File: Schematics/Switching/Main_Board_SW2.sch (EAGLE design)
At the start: 83 parts, among them IC3 SWITCHER, IC4 SWITCHER, Q1 32.768kHz, X1 MINI-USB-SHIELD-UX60-MB-5ST, X2 RJ45

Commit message: PCB Push
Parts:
- added R28, R29: 5.6k, rcl:R-US_R0805
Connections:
- new net N$22: R28.1, R29.2, U$1.5
- net GND: now also R29.1
- net V+: now also R28.2
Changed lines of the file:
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@@
 <?xml version="1.0" encoding="utf-8"?>
 <!DOCTYPE eagle SYSTEM "eagle.dtd">
-<eagle version="6.5.0">
+<eagle version="6.3">
 <drawing>
 <settings>
@@
 <grid distance="0.1" unitdist="inch" unit="inch" style="lines" multiple="1" display="no" altdistance="0.01" altunitdist="inch" altunit="inch"/>
 <layers>
-<layer number="1" name="Top" color="4" fill="1" visible="no" active="no"/>
-<layer number="16" name="Bottom" color="1" fill="1" visible="no" active="no"/>
-<layer number="17" name="Pads" color="2" fill="1" visible="no" active="no"/>
-<layer number="18" name="Vias" color="2" fill="1" visible="no" active="no"/>
-<layer number="19" name="Unrouted" color="6" fill="1" visible="no" active="no"/>
-<layer number="20" name="Dimension" color="15" fill="1" visible="no" active="no"/>
-<layer number="21" name="tPlace" color="7" fill="1" visible="no" active="no"/>
-<layer number="22" name="bPlace" color="7" fill="1" visible="no" active="no"/>
-<layer number="23" name="tOrigins" color="15" fill="1" visible="no" active="no"/>
-<layer number="24" name="bOrigins" color="15" fill="1" visible="no" active="no"/>
-<layer number="25" name="tNames" color="7" fill="1" visible="no" active="no"/>
-<layer number="26" name="bNames" color="7" fill="1" visible="no" active="no"/>
-<layer number="27" name="tValues" color="7" fill="1" visible="no" active="no"/>
-<layer number="28" name="bValues" color="7" fill="1" visible="no" active="no"/>
+<layer number="1" name="Top" color="4" fill="1" visible="yes" active="no"/>
+<layer number="16" name="Bottom" color="1" fill="1" visible="yes" active="no"/>
+<layer number="17" name="Pads" color="2" fill="1" visible="yes" active="no"/>
+<layer number="18" name="Vias" color="2" fill="1" visible="yes" active="no"/>
+<layer number="19" name="Unrouted" color="6" fill="1" visible="yes" active="no"/>
+<layer number="20" name="Dimension" color="15" fill="1" visible="yes" active="no"/>
+<layer number="21" name="tPlace" color="7" fill="1" visible="yes" active="no"/>
+<layer number="22" name="bPlace" color="7" fill="1" visible="yes" active="no"/>
+<layer number="23" name="tOrigins" color="15" fill="1" visible="yes" active="no"/>
+<layer number="24" name="bOrigins" color="15" fill="1" visible="yes" active="no"/>
+<layer number="25" name="tNames" color="7" fill="1" visible="yes" active="no"/>
+<layer number="26" name="bNames" color="7" fill="1" visible="yes" active="no"/>
+<layer number="27" name="tValues" color="7" fill="1" visible="yes" active="no"/>
+<layer number="28" name="bValues" color="7" fill="1" visible="yes" active="no"/>
 <layer number="29" name="tStop" color="7" fill="3" visible="no" active="no"/>
 <layer number="30" name="bStop" color="7" fill="6" visible="no" active="no"/>
@@
 <layer number="35" name="tGlue" color="7" fill="4" visible="no" active="no"/>
 <layer number="36" name="bGlue" color="7" fill="5" visible="no" active="no"/>
-<layer number="37" name="tTest" color="7" fill="1" visible="no" active="no"/>
-<layer number="38" name="bTest" color="7" fill="1" visible="no" active="no"/>
+<layer number="37" name="tTest" color="7" fill="1" visible="yes" active="no"/>
+<layer number="38" name="bTest" color="7" fill="1" visible="yes" active="no"/>
 <layer number="39" name="tKeepout" color="4" fill="11" visible="no" active="no"/>
 <layer number="40" name="bKeepout" color="1" fill="11" visible="no" active="no"/>
@@
 <layer number="44" name="Drills" color="7" fill="1" visible="no" active="no"/>
 <layer number="45" name="Holes" color="7" fill="1" visible="no" active="no"/>
-<layer number="46" name="Milling" color="3" fill="1" visible="no" active="no"/>
-<layer number="47" name="Measures" color="7" fill="1" visible="no" active="no"/>
-<layer number="48" name="Document" color="7" fill="1" visible="no" active="no"/>
-<layer number="49" name="Reference" color="7" fill="1" visible="no" active="no"/>
-<layer number="50" name="dxf" color="7" fill="1" visible="no" active="no"/>
-<layer number="51" name="tDocu" color="7" fill="1" visible="no" active="no"/>
-<layer number="52" name="bDocu" color="7" fill="1" visible="no" active="no"/>
-<layer number="53" name="tGND_GNDA" color="7" fill="1" visible="no" active="no"/>
-<layer number="54" name="bGND_GNDA" color="7" fill="1" visible="no" active="no"/>
-<layer number="56" name="wert" color="7" fill="1" visible="no" active="no"/>
+<layer number="46" name="Milling" color="3" fill="1" visible="yes" active="no"/>
+<layer number="47" name="Measures" color="7" fill="1" visible="yes" active="no"/>
+<layer number="48" name="Document" color="7" fill="1" visible="yes" active="no"/>
+<layer number="49" name="Reference" color="7" fill="1" visible="yes" active="no"/>
+<layer number="50" name="dxf" color="7" fill="1" visible="yes" active="no"/>
+<layer number="51" name="tDocu" color="7" fill="1" visible="yes" active="no"/>
+<layer number="52" name="bDocu" color="7" fill="1" visible="yes" active="no"/>
+<layer number="53" name="tGND_GNDA" color="7" fill="1" visible="yes" active="no"/>
+<layer number="54" name="bGND_GNDA" color="7" fill="1" visible="yes" active="no"/>
+<layer number="56" name="wert" color="7" fill="1" visible="yes" active="no"/>
 <layer number="91" name="Nets" color="2" fill="1" visible="yes" active="yes"/>
 <layer number="92" name="Busses" color="1" fill="1" visible="yes" active="yes"/>
@@
 <part name="H3" library="holes" deviceset="MOUNT-HOLE" device="2.8"/>
 <part name="H4" library="holes" deviceset="MOUNT-HOLE" device="2.8"/>
+<part name="R28" library="rcl" deviceset="R-US_" device="R0805" value="5.6k"/>
+<part name="R29" library="rcl" deviceset="R-US_" device="R0805" value="5.6k"/>
+<part name="SUPPLY1" library="supply2" deviceset="V+" device=""/>
+<part name="GND14" library="supply1" deviceset="GND" device=""/>
 </parts>
 <sheets>
@@
 <instance part="H3" gate="G$1" x="185.42" y="0"/>
 <instance part="H4" gate="G$1" x="185.42" y="-5.08"/>
+<instance part="R28" gate="G$1" x="10.16" y="68.58" smashed="yes" rot="R90">
+<attribute name="NAME" x="8.6614" y="64.77" size="1.778" layer="95" rot="R90"/>
+<attribute name="VALUE" x="13.462" y="64.77" size="1.778" layer="96" rot="R90"/>
+</instance>
+<instance part="R29" gate="G$1" x="10.16" y="55.88" smashed="yes" rot="R90">
+<attribute name="NAME" x="8.6614" y="52.07" size="1.778" layer="95" rot="R90"/>
+<attribute name="VALUE" x="13.462" y="52.07" size="1.778" layer="96" rot="R90"/>
+</instance>
+<instance part="SUPPLY1" gate="1" x="10.16" y="78.74"/>
+<instance part="GND14" gate="1" x="10.16" y="45.72"/>
 </instances>
 <busses>
@@
 <junction x="109.22" y="68.58"/>
 </segment>
+<segment>
+<pinref part="GND14" gate="1" pin="GND"/>
+<pinref part="R29" gate="G$1" pin="1"/>
+<wire x1="10.16" y1="50.8" x2="10.16" y2="48.26" width="0.1524" layer="91"/>
+</segment>
 </net>
 <net name="N$11" class="0">
@@
 <pinref part="SUPPLY8" gate="1" pin="V+"/>
 </segment>
+<segment>
+<pinref part="SUPPLY1" gate="1" pin="V+"/>
+<pinref part="R28" gate="G$1" pin="2"/>
+<wire x1="10.16" y1="76.2" x2="10.16" y2="73.66" width="0.1524" layer="91"/>
+</segment>
 </net>
 <net name="N$13" class="0">
@@
 </segment>
 </net>
+<net name="N$22" class="0">
+<segment>
+<wire x1="15.24" y1="60.96" x2="15.24" y2="81.28" width="0.1524" layer="91"/>
+<pinref part="R28" gate="G$1" pin="1"/>
+<pinref part="R29" gate="G$1" pin="2"/>
+<wire x1="10.16" y1="60.96" x2="10.16" y2="63.5" width="0.1524" layer="91"/>
+<wire x1="10.16" y1="60.96" x2="15.24" y2="60.96" width="0.1524" layer="91"/>
+<junction x="10.16" y="60.96"/>
+<wire x1="15.24" y1="81.28" x2="33.02" y2="81.28" width="0.1524" layer="91"/>
+<wire x1="33.02" y1="81.28" x2="33.02" y2="63.5" width="0.1524" layer="91"/>
+<pinref part="U$1" gate="G$1" pin="5"/>
+<wire x1="33.02" y1="63.5" x2="53.34" y2="63.5" width="0.1524" layer="91"/>
+</segment>
+</net>

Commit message: PCB Verified. Add Battery Sense
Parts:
- R16, R19: device resistor:R-US_R1206 -> resistor:R-US_R0805
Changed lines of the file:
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@@
 <part name="IC3" library="linear-technology-2" deviceset="SWITCHER" device=""/>
 <part name="SUPPLY4" library="supply2" deviceset="V+" device=""/>
-<part name="R16" library="resistor" deviceset="R-US_" device="R1206" value="499K"/>
+<part name="R16" library="resistor" deviceset="R-US_" device="R0805" value="499K"/>
 <part name="R17" library="rcl" deviceset="R-US_" device="R0805" value="10k"/>
 <part name="L1" library="Inductor" deviceset="SHEILDED_COIL" device="" value="4.7uH"/>
@@
 <part name="IC4" library="linear-technology-2" deviceset="SWITCHER" device=""/>
 <part name="SUPPLY6" library="supply2" deviceset="V+" device=""/>
-<part name="R19" library="resistor" deviceset="R-US_" device="R1206" value="499k"/>
+<part name="R19" library="resistor" deviceset="R-US_" device="R0805" value="499k"/>
 <part name="R20" library="rcl" deviceset="R-US_" device="R0805" value="10k"/>
 <part name="L2" library="Inductor" deviceset="SHEILDED_COIL" device="" value="4.7uH"/>

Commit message: Last layout sync of night
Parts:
- L1: value 4.7uH -> 3.3uH
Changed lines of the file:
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@@
 <?xml version="1.0" encoding="utf-8"?>
 <!DOCTYPE eagle SYSTEM "eagle.dtd">
-<eagle version="6.3">
+<eagle version="6.4">
 <drawing>
 <settings>
@@
 <grid distance="0.1" unitdist="inch" unit="inch" style="lines" multiple="1" display="no" altdistance="0.01" altunitdist="inch" altunit="inch"/>
 <layers>
-<layer number="1" name="Top" color="4" fill="1" visible="yes" active="no"/>
-<layer number="16" name="Bottom" color="1" fill="1" visible="yes" active="no"/>
-<layer number="17" name="Pads" color="2" fill="1" visible="yes" active="no"/>
-<layer number="18" name="Vias" color="2" fill="1" visible="yes" active="no"/>
-<layer number="19" name="Unrouted" color="6" fill="1" visible="yes" active="no"/>
-<layer number="20" name="Dimension" color="15" fill="1" visible="yes" active="no"/>
-<layer number="21" name="tPlace" color="7" fill="1" visible="yes" active="no"/>
-<layer number="22" name="bPlace" color="7" fill="1" visible="yes" active="no"/>
-<layer number="23" name="tOrigins" color="15" fill="1" visible="yes" active="no"/>
-<layer number="24" name="bOrigins" color="15" fill="1" visible="yes" active="no"/>
-<layer number="25" name="tNames" color="7" fill="1" visible="yes" active="no"/>
-<layer number="26" name="bNames" color="7" fill="1" visible="yes" active="no"/>
-<layer number="27" name="tValues" color="7" fill="1" visible="yes" active="no"/>
-<layer number="28" name="bValues" color="7" fill="1" visible="yes" active="no"/>
+<layer number="1" name="Top" color="4" fill="1" visible="no" active="no"/>
+<layer number="16" name="Bottom" color="1" fill="1" visible="no" active="no"/>
+<layer number="17" name="Pads" color="2" fill="1" visible="no" active="no"/>
+<layer number="18" name="Vias" color="2" fill="1" visible="no" active="no"/>
+<layer number="19" name="Unrouted" color="6" fill="1" visible="no" active="no"/>
+<layer number="20" name="Dimension" color="15" fill="1" visible="no" active="no"/>
+<layer number="21" name="tPlace" color="7" fill="1" visible="no" active="no"/>
+<layer number="22" name="bPlace" color="7" fill="1" visible="no" active="no"/>
+<layer number="23" name="tOrigins" color="15" fill="1" visible="no" active="no"/>
+<layer number="24" name="bOrigins" color="15" fill="1" visible="no" active="no"/>
+<layer number="25" name="tNames" color="7" fill="1" visible="no" active="no"/>
+<layer number="26" name="bNames" color="7" fill="1" visible="no" active="no"/>
+<layer number="27" name="tValues" color="7" fill="1" visible="no" active="no"/>
+<layer number="28" name="bValues" color="7" fill="1" visible="no" active="no"/>
 <layer number="29" name="tStop" color="7" fill="3" visible="no" active="no"/>
 <layer number="30" name="bStop" color="7" fill="6" visible="no" active="no"/>
@@
 <layer number="35" name="tGlue" color="7" fill="4" visible="no" active="no"/>
 <layer number="36" name="bGlue" color="7" fill="5" visible="no" active="no"/>
-<layer number="37" name="tTest" color="7" fill="1" visible="yes" active="no"/>
-<layer number="38" name="bTest" color="7" fill="1" visible="yes" active="no"/>
+<layer number="37" name="tTest" color="7" fill="1" visible="no" active="no"/>
+<layer number="38" name="bTest" color="7" fill="1" visible="no" active="no"/>
 <layer number="39" name="tKeepout" color="4" fill="11" visible="no" active="no"/>
 <layer number="40" name="bKeepout" color="1" fill="11" visible="no" active="no"/>
@@
 <layer number="44" name="Drills" color="7" fill="1" visible="no" active="no"/>
 <layer number="45" name="Holes" color="7" fill="1" visible="no" active="no"/>
-<layer number="46" name="Milling" color="3" fill="1" visible="yes" active="no"/>
-<layer number="47" name="Measures" color="7" fill="1" visible="yes" active="no"/>
-<layer number="48" name="Document" color="7" fill="1" visible="yes" active="no"/>
-<layer number="49" name="Reference" color="7" fill="1" visible="yes" active="no"/>
-<layer number="50" name="dxf" color="7" fill="1" visible="yes" active="no"/>
-<layer number="51" name="tDocu" color="7" fill="1" visible="yes" active="no"/>
-<layer number="52" name="bDocu" color="7" fill="1" visible="yes" active="no"/>
-<layer number="53" name="tGND_GNDA" color="7" fill="1" visible="yes" active="no"/>
-<layer number="54" name="bGND_GNDA" color="7" fill="1" visible="yes" active="no"/>
-<layer number="56" name="wert" color="7" fill="1" visible="yes" active="no"/>
+<layer number="46" name="Milling" color="3" fill="1" visible="no" active="no"/>
+<layer number="47" name="Measures" color="7" fill="1" visible="no" active="no"/>
+<layer number="48" name="Document" color="7" fill="1" visible="no" active="no"/>
+<layer number="49" name="Reference" color="7" fill="1" visible="no" active="no"/>
+<layer number="50" name="dxf" color="7" fill="1" visible="no" active="no"/>
+<layer number="51" name="tDocu" color="7" fill="1" visible="no" active="no"/>
+<layer number="52" name="bDocu" color="7" fill="1" visible="no" active="no"/>
+<layer number="53" name="tGND_GNDA" color="7" fill="1" visible="no" active="no"/>
+<layer number="54" name="bGND_GNDA" color="7" fill="1" visible="no" active="no"/>
+<layer number="56" name="wert" color="7" fill="1" visible="no" active="no"/>
 <layer number="91" name="Nets" color="2" fill="1" visible="yes" active="yes"/>
 <layer number="92" name="Busses" color="1" fill="1" visible="yes" active="yes"/>
@@
 <part name="R16" library="resistor" deviceset="R-US_" device="R0805" value="499K"/>
 <part name="R17" library="rcl" deviceset="R-US_" device="R0805" value="10k"/>
-<part name="L1" library="Inductor" deviceset="SHEILDED_COIL" device="" value="4.7uH"/>
+<part name="L1" library="Inductor" deviceset="SHEILDED_COIL" device="" value="3.3uH"/>
 <part name="D6" library="diode" deviceset="DIODE-" device="SOD323-R"/>
 <part name="D7" library="diode" deviceset="DIODE-" device="SOD323-R"/>

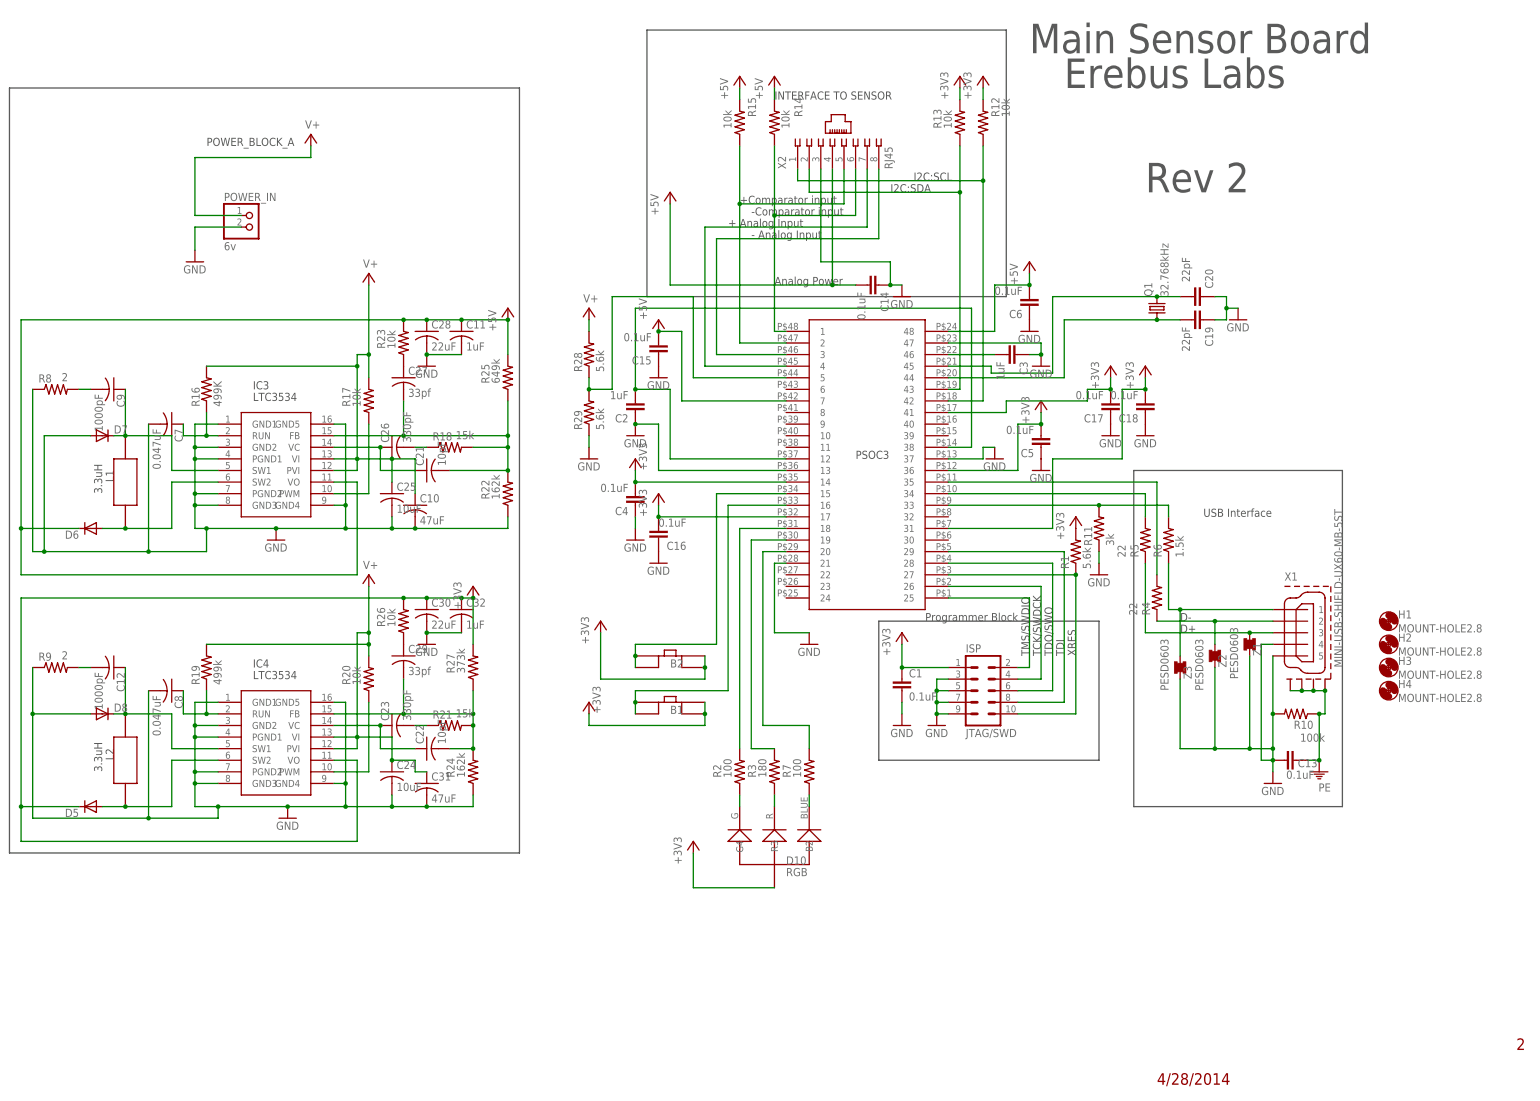
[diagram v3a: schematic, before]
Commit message: Cleaned up stuff
Made Schematics easier to read
Split Supplies in BOM and made names match references
Renamed parts on sensor
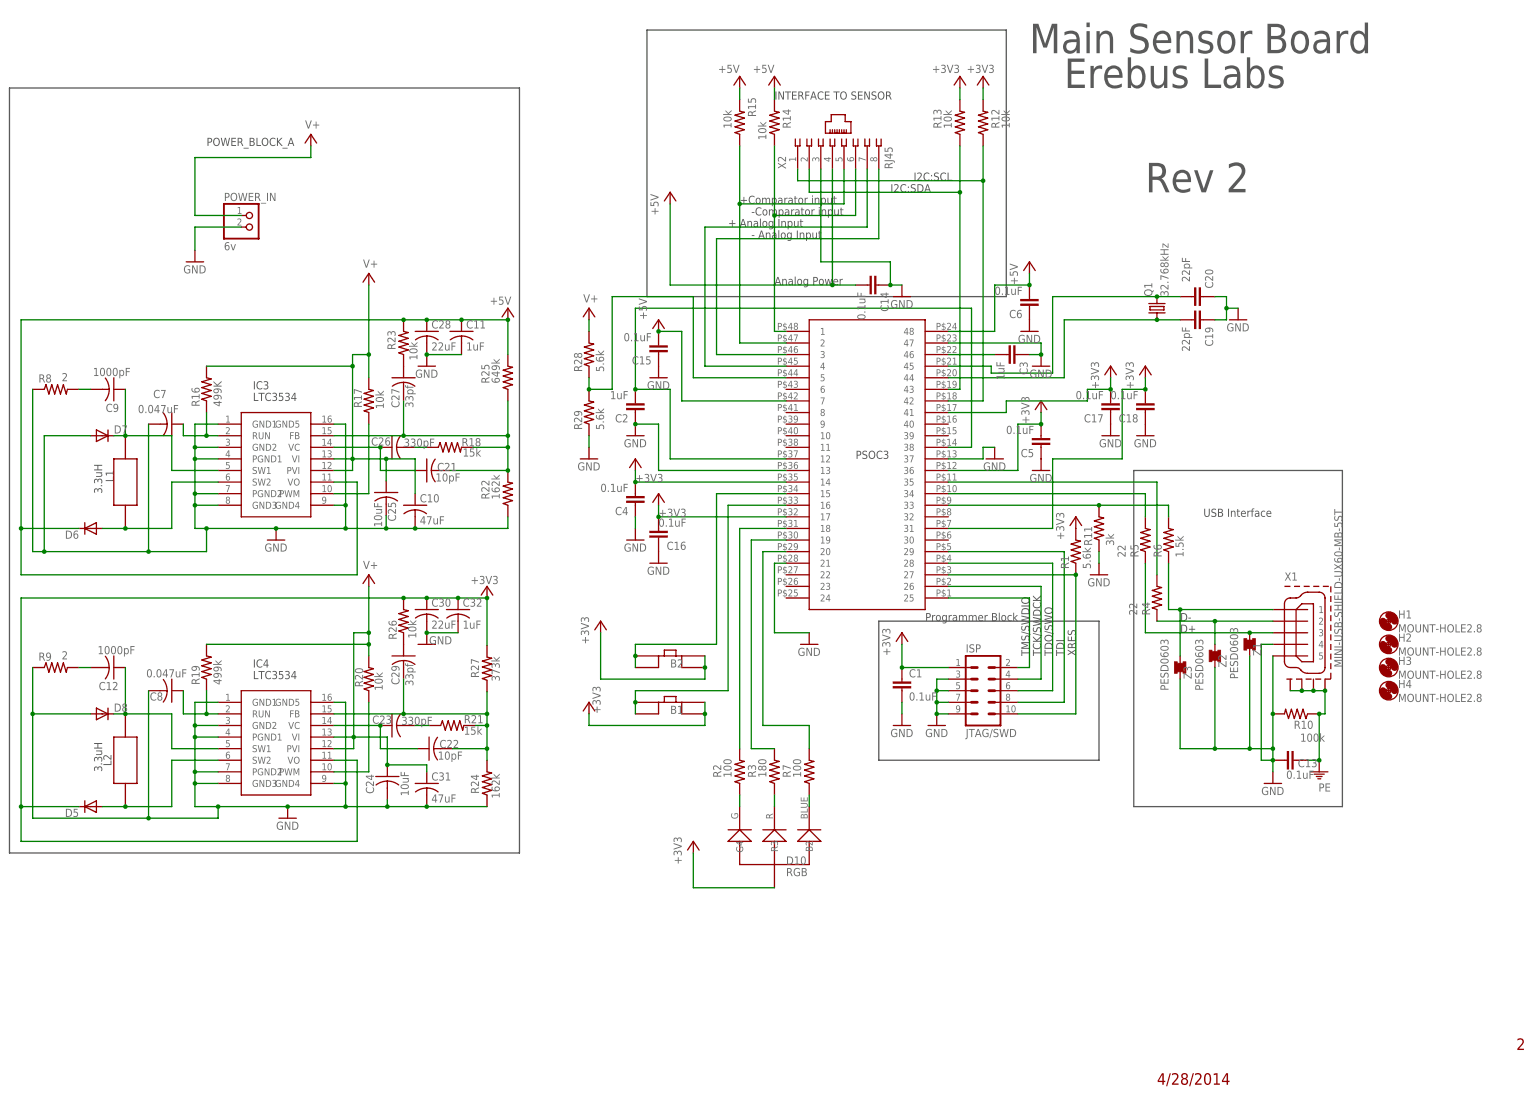
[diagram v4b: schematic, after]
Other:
- moved on the sheet: C22, C24, C25, C32, R21, R24, R27
